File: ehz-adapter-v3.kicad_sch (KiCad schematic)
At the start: 20 parts

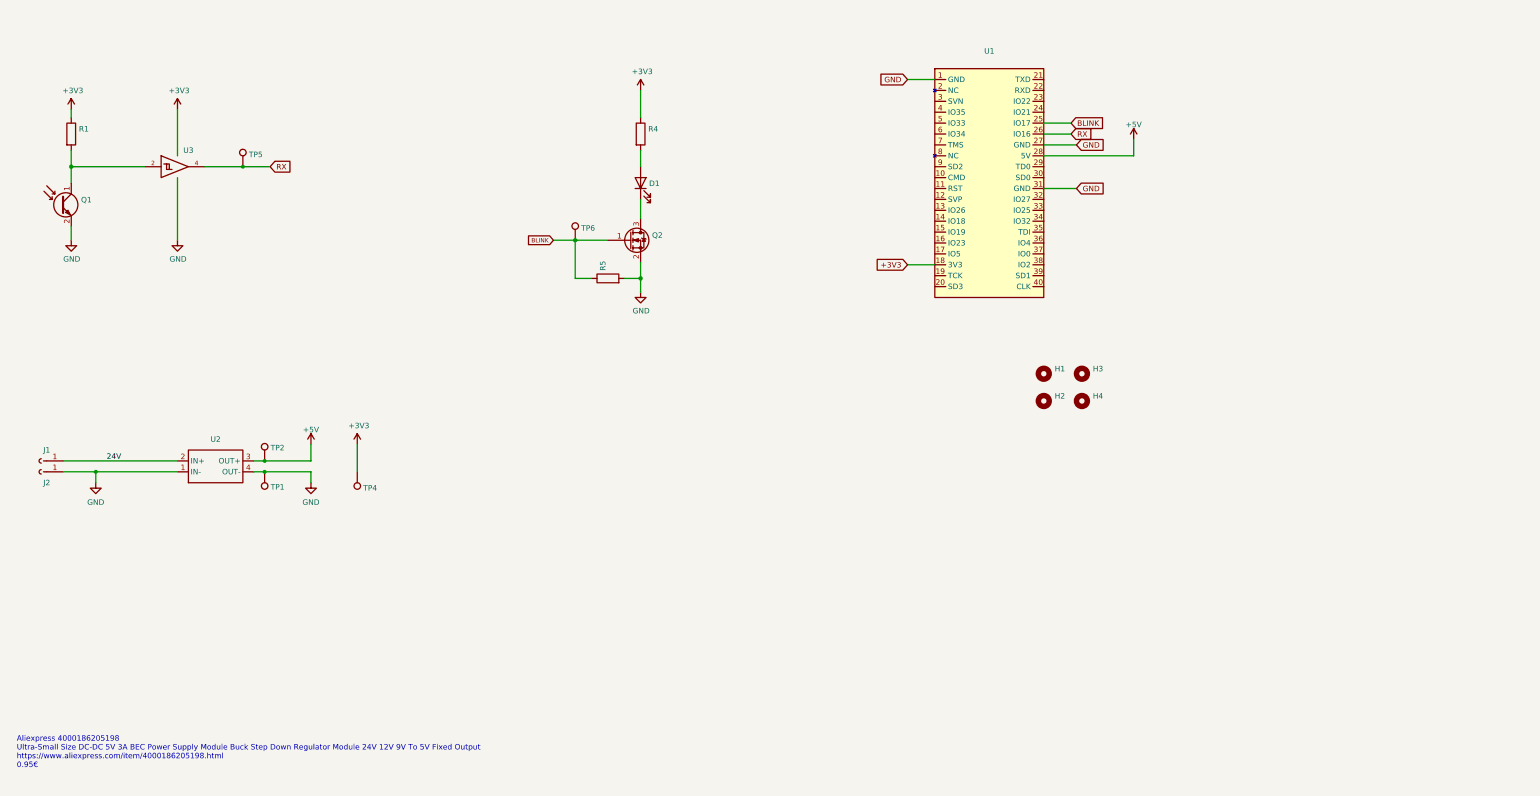
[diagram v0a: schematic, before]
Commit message: Many changes to use ESP32 WROOM
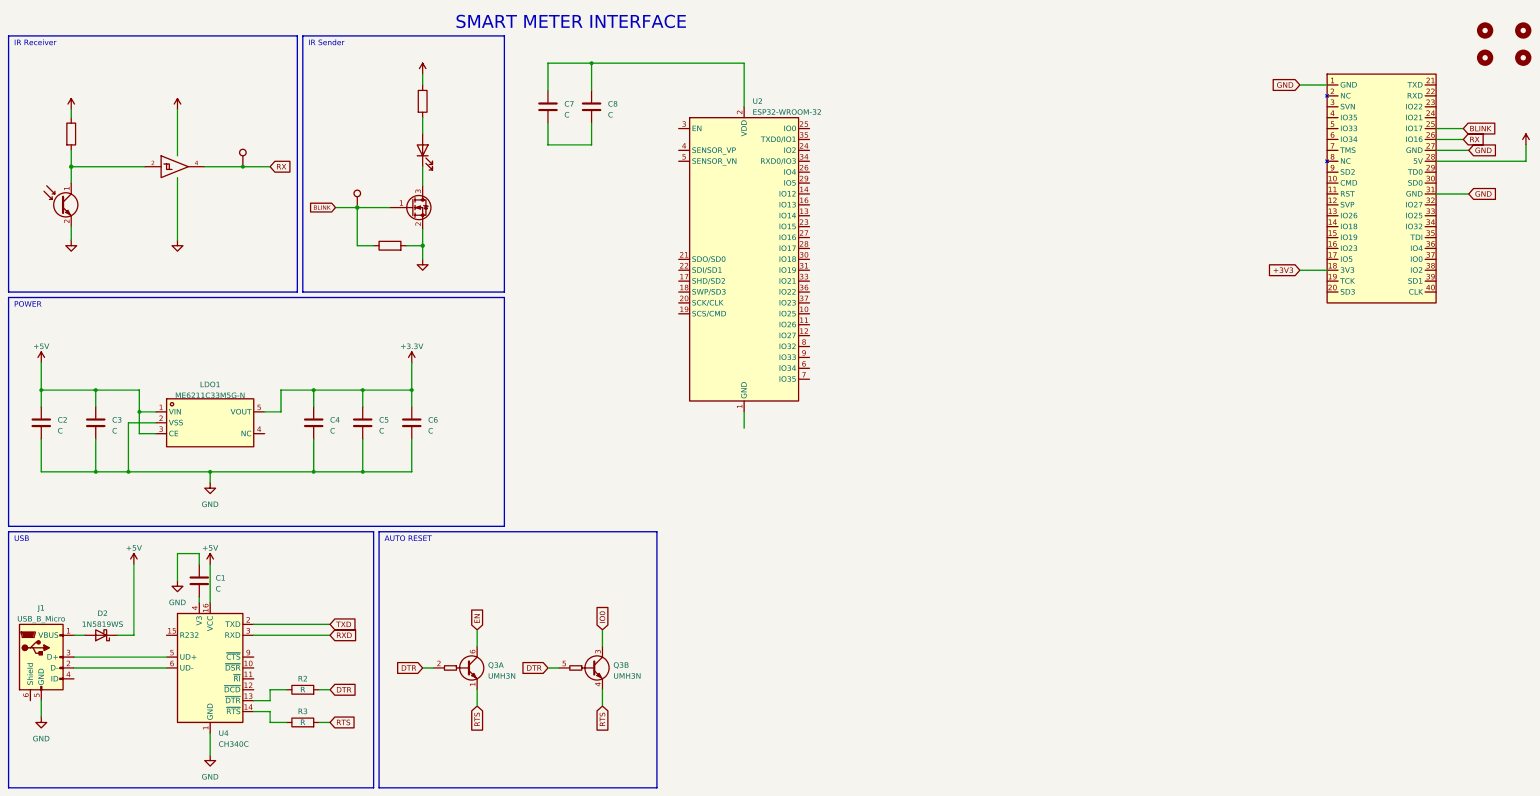
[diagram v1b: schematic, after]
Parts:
- removed J1, J2: (no value), symbol Connector:Conn_01x01_Female
- removed TP1, TP2, TP4: (no value), symbol Connector:TestPoint
- removed U2: (no value), symbol bouni:DC-DC-BOARD
- added C1, C2, C3, C4, C5, C6, C7, C8: C, symbol Device:C
- added D2: 1N5819WS, Diode_SMD:D_SOD-323, symbol Diode:1N5819WS
- added J1: USB_B_Micro, symbol Connector:USB_B_Micro
- added LDO1: ME6211C33M5G-N, LCSC:SOT-23-5_L3.0-W1.7-P0.95-LS2.8-BR, symbol LCSC:ME6211C33M5G-N
- added Q3: UMH3N, Package_TO_SOT_SMD:SOT-363_SC-70-6, symbol Transistor_BJT:UMH3N
- added R2, R3: R, symbol Device:R
- added U2: ESP32-WROOM-32, RF_Module:ESP32-WROOM-32, symbol RF_Module:ESP32-WROOM-32
- added U4: CH340C, Package_SO:SOIC-16_3.9x9.9mm_P1.27mm, symbol Interface_USB:CH340C
- ?: renamed from D1; LCSC (none) -> C131280
- ?: renamed from Q1; LCSC (none) -> C131248
- renumbered Q2 to ?, R1 to ?, R4 to ?, U3 to ?, H1 to ?, H3 to ?, TP6 to ?, H2 to ?, U1 to ?, R5 to ?, TP5 to ?, H4 to ?
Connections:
- net +5V: now also C2.1, C3.1, D2.1 (K), LDO1.1 (VIN), LDO1.3 (CE), U4.16 (VCC)
- net GND: now also C1.1, C2.2, C3.2, C4.2, C5.2, C6.2, J1.5 (GND), LDO1.2 (VSS), U4.1 (GND)
- new net: D2.2 (A), J1.1 (VBUS)
- new net: J1.2 (D-), U4.6 (UD-)
- new net: J1.3 (D+), U4.5 (UD+)
- new net: C1.2, U4.4 (V3)
- new net: U2.1 (GND), U2.15 (GND), U2.38 (GND), U2.39 (GND)
- new net: C7.1, C8.1, U2.2 (VDD)
- new net: C7.2, C8.2
- new net: R2.1, U4.13 (~{DTR})
- new net: R3.1, U4.14 (~{RTS})
- new net +3.3V: C4.1, C5.1, C6.1, LDO1.5 (VOUT)
- new net DTR: Q3.2 (B1), Q3.5 (B2), R2.2
- new net EN: Q3.6 (C1)
- new net IO0: Q3.3 (C2)
- new net RTS: Q3.1 (E1), Q3.4 (E2), R3.2
- new net RXD: U4.3 (RXD)
- new net TXD: U4.2 (TXD)
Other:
- note added: "AUTO RESET"
- note added: "IR Receiver"
- note added: "IR Sender"
- note added: "POWER"
- note added: "SMART METER INTERFACE"
- note added: "USB"
- note removed: "Aliexpress 4000186205198 Ultra-Small Size DC-DC 5V 3A BEC Power Supply Module Buck Step Down Regulator Module 24V 12V 9V To 5V Fixed Output https://www.aliexpress.com/item/4000186205198.html 0.95€"
